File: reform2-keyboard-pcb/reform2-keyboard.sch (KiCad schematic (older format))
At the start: 164 parts, among them SW1 Choc, SW10 Choc, SW11 Choc, SW12 Choc, SW13 Choc, SW14 Choc, SW15 Choc, SW16 Choc, SW17 Choc, SW18 Choc, SW19 Choc, SW2 Choc, SW20 Choc, SW21 Choc, SW22 Choc, SW23 Choc, SW24 Choc, SW25 Choc, SW26 Choc, SW27 Choc, SW28 Choc, SW29 Choc, SW3 Choc, SW30 Choc, SW31 Choc, SW32 Choc, SW33 Choc, SW34 Choc, SW35 Choc, SW36 Choc, SW37 Choc, SW38 Choc, SW39 Choc, SW4 Choc, SW40 Choc, SW41 Choc, SW42 Choc, SW43 Choc, SW44 Choc, SW45 Choc, SW46 Choc, SW47 Choc, SW48 Choc, SW49 Choc, SW5 Choc, SW50 Choc, SW51 Choc, SW52 Choc, SW53 Choc, SW54 Choc, SW55 Choc, SW56 Choc, SW57 Choc, SW58 Choc, SW59 Choc, SW6 Choc, SW60 Choc, SW61 Choc, SW62 Choc, SW63 Choc, SW64 Choc, SW65 Choc, SW66 Choc, SW67 Choc, SW68 Choc, SW69 Choc, SW7 Choc, SW70 Choc, SW71 Choc, SW72 Choc, SW73 Choc, SW74 Choc, SW75 Choc, SW76 Choc, SW77 Choc, SW78 Choc, SW79 Choc, SW8 Choc, SW80 Choc, SW81 Choc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

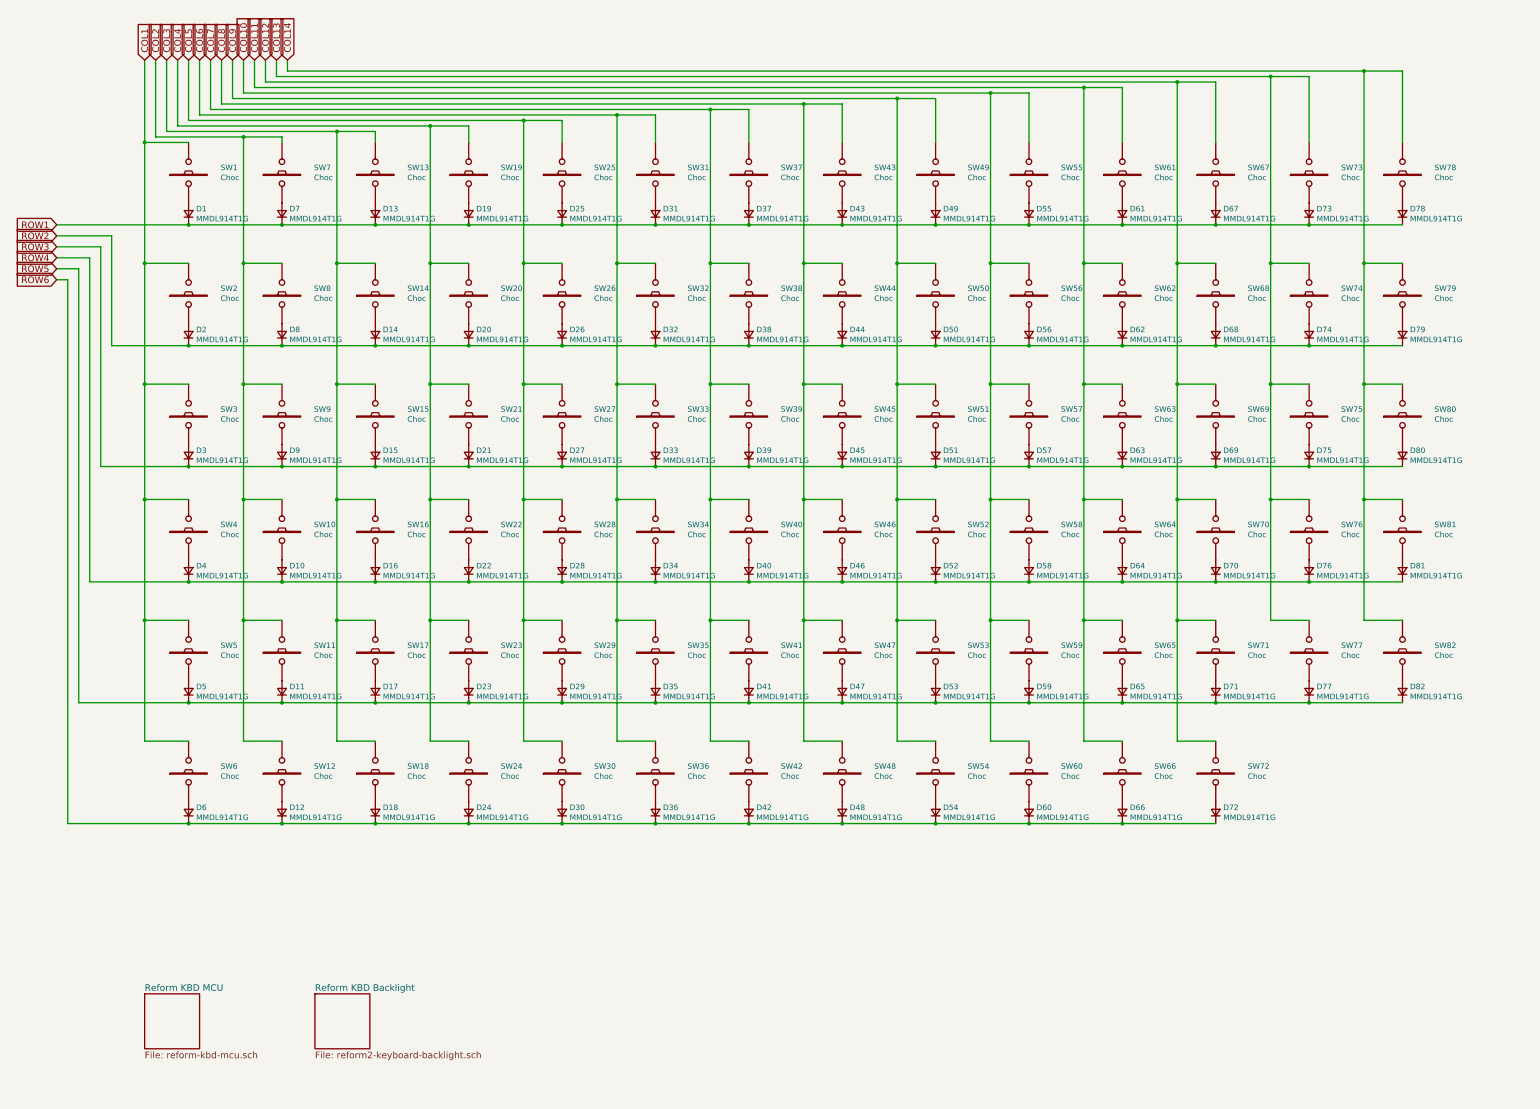
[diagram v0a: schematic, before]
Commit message: reform2: update PCBs incl. badges to production revs, add keyboard lettering, misc docs
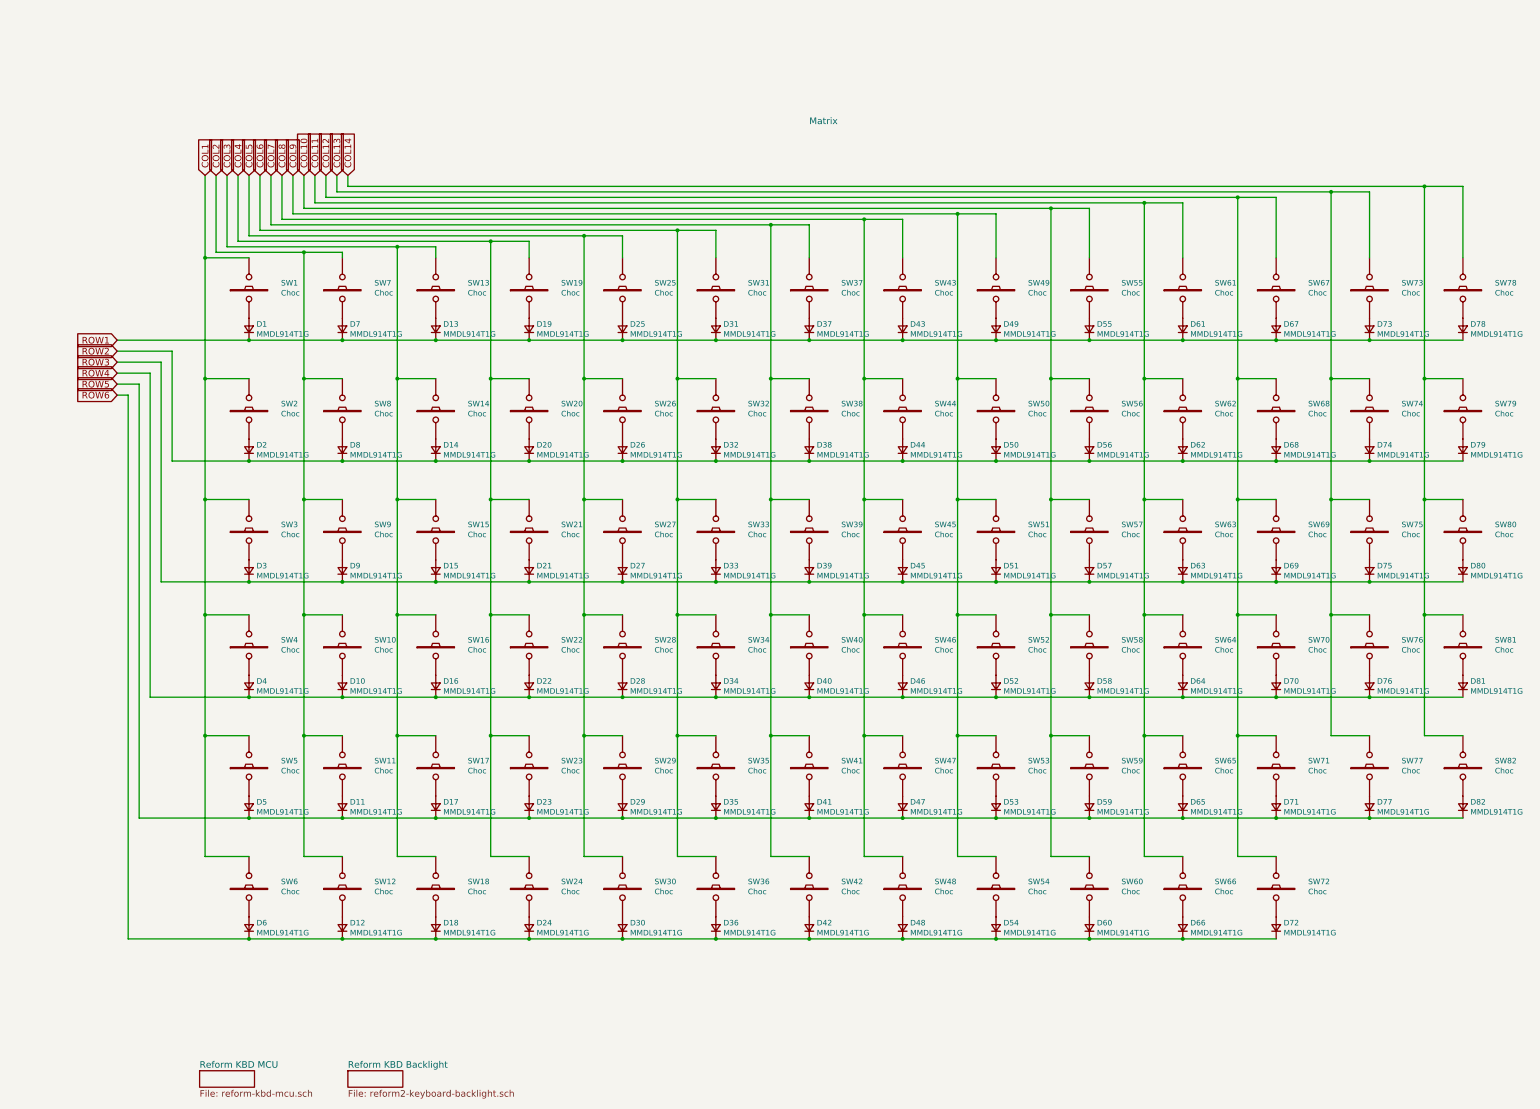
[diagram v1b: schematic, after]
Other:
- note added: "Matrix"
- moved on the sheet: D1, D10, D11, D12, D13, D14, D15, D16, D17, D18, D19, D2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

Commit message: keyboard: add pcb version that has almost all components on the front side, with parts from lcsc
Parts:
- D1, D10, D11, D12, D13, D14, D15, D16, D17, D18, D19, D2, D20, D21, D22, D23, D24, D25, D26, D27, D28, D29, D3, D30, D31, D32, D33, D34, D35, D36, D37, D38, D39, D4, D40, D41, D42, D43, D44, D45, D46, D47, D48, D49, D5, D50, D51, D52, D53, D54, D55, D56, D57, D58, D59, D6, D60, D61, D62, D63, D64, D65, D66, D67, D68, D69, D7, D70, D71, D72, D73, D74, D75, D76, D77, D78, D79, D8, D80, D81, D82, D9: Alt MPN (none) -> MMDL914T1G; Alt Manuf (none) -> On; LCSC (none) -> C193404; Manufacturer ON -> MDD; Manufacturer_No MMDL914T1G -> 1N4007WS
- SW1, SW10, SW11, SW12, SW13, SW14, SW15, SW16, SW17, SW18, SW19, SW2, SW20, SW21, SW22, SW23, SW24, SW25, SW26, SW27, SW28, SW29, SW3, SW30, SW31, SW32, SW33, SW34, SW35, SW36, SW37, SW38, SW39, SW4, SW40, SW41, SW42, SW43, SW44, SW45, SW46, SW47, SW48, SW49, SW5, SW50, SW51, SW52, SW53, SW54, SW55, SW56, SW57, SW58, SW59, SW6, SW60, SW61, SW62, SW63, SW64, SW65, SW66, SW67, SW68, SW69, SW7, SW70, SW71, SW72, SW73, SW74, SW75, SW76, SW77, SW78, SW79, SW8, SW80, SW81, SW82, SW9: LCSC (none) -> C400230
